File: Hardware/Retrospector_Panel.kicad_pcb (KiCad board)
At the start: 2 copper layers, 60.8 x 128.5 mm, 43 parts, among them J1 Audio_In_L, J10 Feedback_CV, J11 Audio_In_R, J12 Audio_Out_R, J13 Audio_Out_L, J2 Delay_CV_L, J7 Mix_CV, J8 Delay_CV_R, J9 Clock

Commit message: Added some test clock code using timer to capture clock interval in capture and compare input mode
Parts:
- removed the Ref** at (143.5, 64.5)
- removed the Ref** at (145.5, 108.5)
- removed the Ref** at (114.5, 108.5)
- removed the Ref** at (130.0, 86.5)
- added DELAY_L: Alpha_9mm_pot_hole, Custom_Footprints:Alpha_9mm_pot_hole, B.Cu at (143.5, 64.5)
- added FEEDBACK: Alpha_9mm_pot_hole, Custom_Footprints:Alpha_9mm_pot_hole, B.Cu at (145.5, 108.5)
- added MIX: Alpha_9mm_pot_hole, Custom_Footprints:Alpha_9mm_pot_hole, B.Cu at (114.5, 108.5)
- added TONE: Alpha_9mm_pot_hole, Custom_Footprints:Alpha_9mm_pot_hole, B.Cu at (130.0, 86.5)
- LED_L, LED_R: renamed from Ref**; footprint Custom_Footprints:Sub_Miniature_Switch_MountingHole_3mm -> Custom_Footprints:LED_Hole_3mm; moved to B.Cu
- MODE, TYPE: renamed from Ref**; moved to B.Cu
- RESET: renamed from Ref**; footprint Custom_Footprints:Sub_Miniature_Switch_MountingHole_3.5mm -> Custom_Footprints:Small_Pushbutton_Hole_3.5mm; moved to B.Cu
- Ref** (x9): moved to B.Cu
- moved D1 536.5 mm to (-267.1, 49.5)
- moved D2 536.5 mm to (-316.6, 49.5)
- moved Delay_Pot_L1 536.5 mm to (-279.6, 63.5)
- moved Delay_Pot_R1 536.5 mm to (-306.6, 63.5)
- moved FXMODE1 536.5 mm to (-307.6, 75.4)
- moved FXTYPE1 536.5 mm to (-274.6, 80.5)
- moved Feedback_Pot1 536.5 mm to (-277.6, 107.5)
- moved J1 536.5 mm to (-269.6, 142.5)
- moved J10 536.5 mm to (-280.1, 125.5)
- moved J11 536.5 mm to (-280.1, 142.5)
- moved J12 536.5 mm to (-311.6, 142.5)
- moved J13 536.5 mm to (-301.1, 142.5)
- moved J2 536.5 mm to (-269.6, 125.5)
- moved J7 536.5 mm to (-301.1, 125.5)
- moved J8 536.5 mm to (-311.6, 125.5)
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- renumbered Ref** to DELAY_R
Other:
- board text removed: "Delay knobs Large unskirted 15.5mm base diameter"
- board text removed: "Mix/Feedback knobs small skirted 14.2mm base diameter"

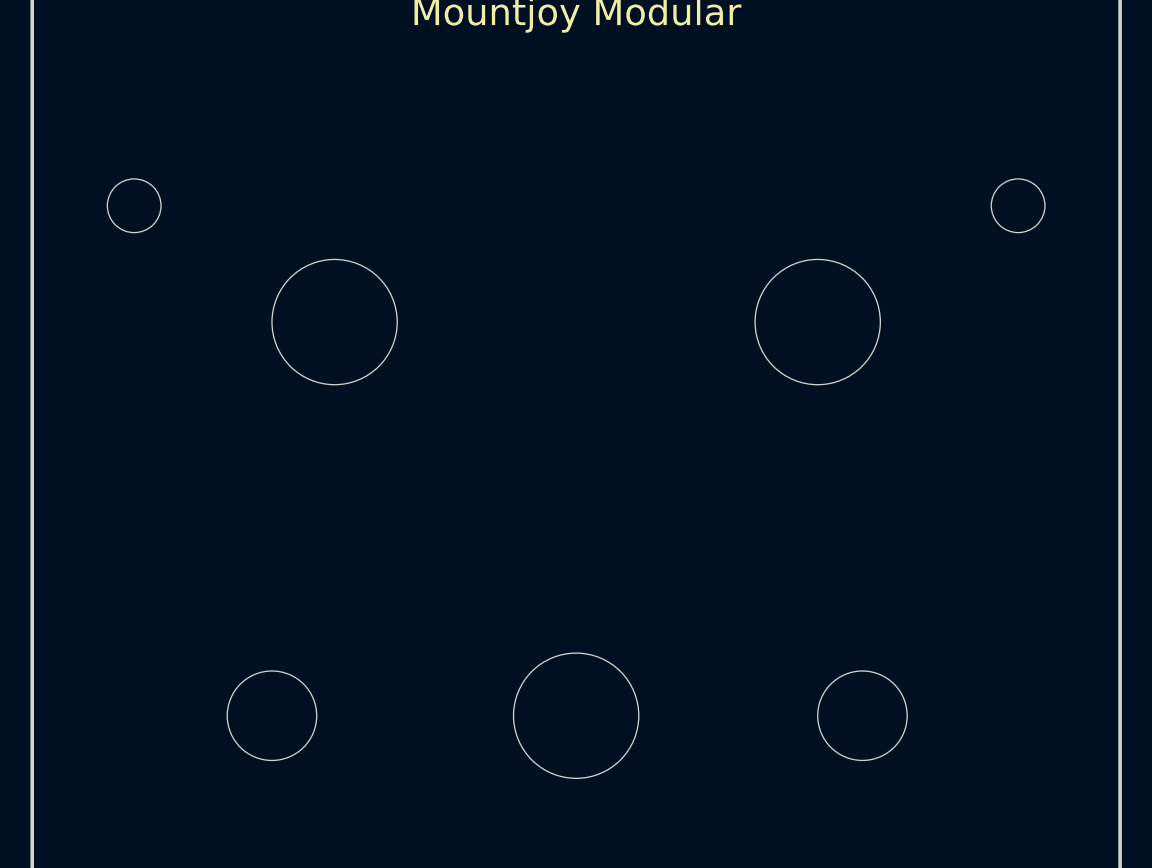
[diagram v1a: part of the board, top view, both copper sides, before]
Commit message: Panel and Control PCB Updates
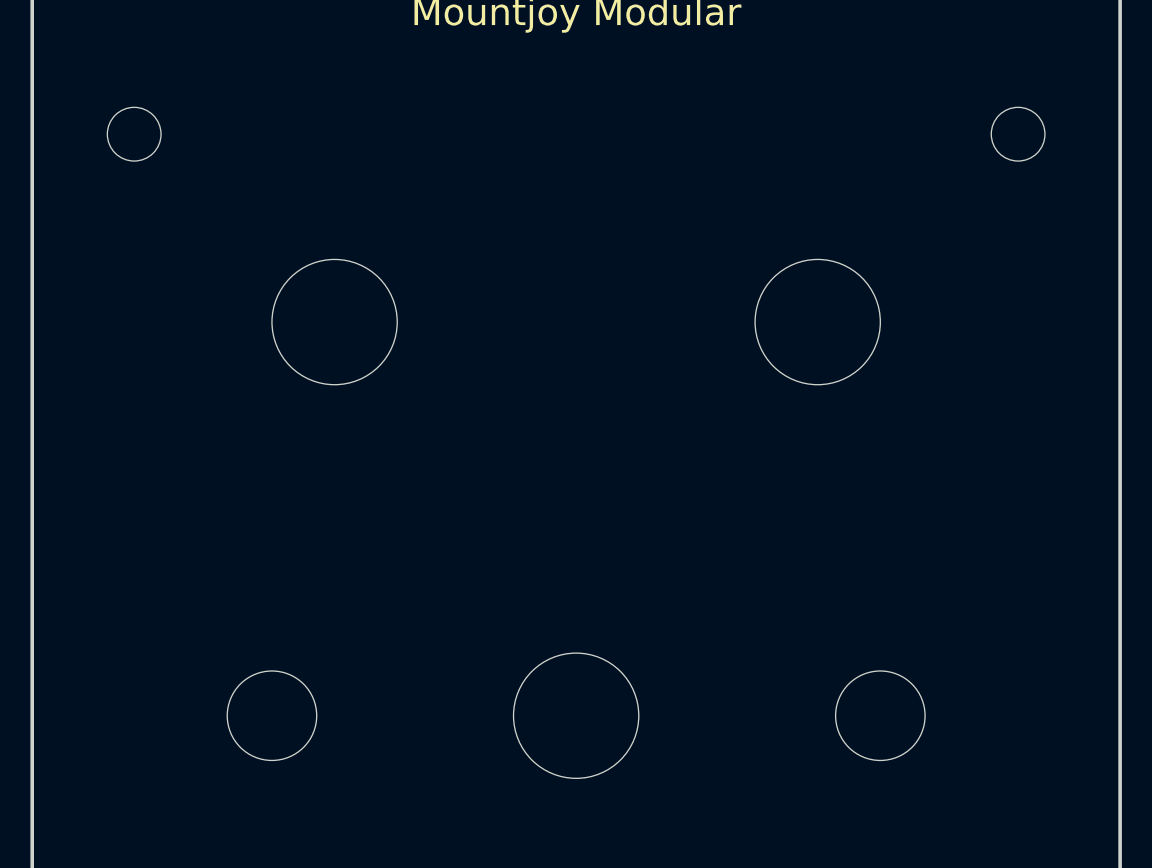
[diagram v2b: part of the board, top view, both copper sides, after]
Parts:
- moved LED_L 4.00 mm to (154.7, 54.0)
- moved LED_R 4.00 mm to (105.3, 54.0)
- moved MODE 1.00 mm to (147.0, 86.5)
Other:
- board text added: "Wet/Dry"
- board text removed: "Delay"
- board text removed: "FB"
- board text removed: "Mix"
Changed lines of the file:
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@@
   (general
     (thickness 1.6)
-    (drawings 68)
+    (drawings 75)
     (tracks 0)
     (zones 0)
@@
   )
   (module Custom_Footprints:Sub_Miniature_Switch_MountingHole_5mm (layer B.Cu)
-    (at 146 86.5)
+    (at 147 86.5)
     (descr "Mounting Hole 6mm, no annular")
     (tags "mounting hole 6mm no annular")
@@
   )
   (module Custom_Footprints:LED_Hole_3mm (layer B.Cu)
-    (at 105.3 58)
+    (at 105.3 54)
     (descr "Mounting Hole 6mm, no annular")
     (tags "mounting hole 6mm no annular")
@@
   )
   (module Custom_Footprints:LED_Hole_3mm (layer B.Cu)
-    (at 154.7 58)
+    (at 154.7 54)
     (descr "Mounting Hole 6mm, no annular")
     (tags "mounting hole 6mm no annular")
@@
     )
   )
-  (gr_line (start 127.5 73) (end 132.5 73) (layer B.Mask) (width 0.4))
-  (gr_line (start 120 76) (end 127.5 73) (layer B.Mask) (width 0.4))
-  (gr_line (start 132.5 73) (end 140 76) (layer B.Mask) (width 0.4))
-  (gr_line (start 120 76) (end 100 76) (layer B.Mask) (width 0.4))
-  (gr_line (start 120 125.5) (end 100 125.5) (layer B.Mask) (width 0.4))
-  (gr_line (start 159.5 125.5) (end 140 125.5) (layer B.Mask) (width 0.4))
-  (gr_line (start 140 125.5) (end 130 123.5) (layer B.Mask) (width 0.4))
-  (gr_line (start 130 123.5) (end 120 125.5) (layer B.Mask) (width 0.4))
-  (gr_line (start 130 51) (end 140 49) (layer B.Mask) (width 0.4))
-  (gr_line (start 120 49) (end 130 51) (layer B.Mask) (width 0.4))
-  (gr_line (start 140 49) (end 160 49) (layer B.Mask) (width 0.4))
-  (gr_line (start 100.5 49) (end 120 49) (layer B.Mask) (width 0.4))
-  (gr_line (start 159.5 76) (end 140 76) (layer B.Mask) (width 0.4))
-  (gr_poly (pts (xy 125 156.9) (xy 103 156.9) (xy 103 145) (xy 125 145)) (layer B.Mask) (width 0.1))
+  (gr_line (start 118.5 77) (end 100 77) (layer B.Mask) (width 0.4))
+  (gr_arc (start 118 63) (end 118 77) (angle -56.08256946) (layer B.Mask) (width 0.4))
+  (gr_arc (start 142.7 63) (end 142.7 49) (angle -180) (layer B.Mask) (width 0.4))
+  (gr_arc (start 118 63.080128) (end 129.6 55.1) (angle -55.47428124) (layer B.Mask) (width 0.4))
+  (gr_line (start 100.5 49) (end 118 49) (layer B.Mask) (width 0.4))
+  (gr_line (start 142 49) (end 160 49) (layer B.Mask) (width 0.4))
+  (gr_line (start 159.5 77) (end 142 77) (layer B.Mask) (width 0.4))
+  (gr_line (start 160.5 96) (end 148.5 96) (layer B.Mask) (width 0.4))
+  (gr_line (start 112 96.08617) (end 100 96.08617) (layer B.Mask) (width 0.4))
+  (gr_line (start 140.5 115) (end 145.5 108.5) (layer B.Mask) (width 0.4))
+  (gr_poly (pts (xy 124 157) (xy 104 157) (xy 104 156) (xy 124 156)) (layer B.Mask) (width 0.1))
+  (gr_poly (pts (xy 124 146.5) (xy 104 146.5) (xy 104 145.5) (xy 124 145.5)) (layer B.Mask) (width 0.1))
+  (gr_circle (center 124 156) (end 124.5 156) (layer B.Mask) (width 1))
+  (gr_circle (center 124 146.5) (end 124.5 146.5) (layer B.Mask) (width 1))
+  (gr_circle (center 104 156) (end 104.5 156) (layer B.Mask) (width 1))
+  (gr_circle (center 104 146.5) (end 104.5 146.5) (layer B.Mask) (width 1))
+  (gr_arc (start 112.000001 111.999999) (end 123 100.5) (angle -43.72697345) (layer B.Mask) (width 0.4))
+  (gr_arc (start 148.100593 111.904836) (end 148.5 96) (angle -45.21155789) (layer B.Mask) (width 0.4))
+  (gr_arc (start 130 93) (end 123 100.5) (angle -86.75204533) (layer B.Mask) (width 0.4))
+  (gr_line (start 114.5 108.5) (end 119.5 115) (layer B.Mask) (width 0.4))
+  (gr_line (start 119.5 115) (end 119.5 134.3) (layer B.Mask) (width 0.4))
+  (gr_line (start 140.5 134) (end 140.5 115) (layer B.Mask) (width 0.4))
+  (gr_line (start 140 150.9) (end 151 150.9) (layer B.Mask) (width 0.4))
+  (gr_line (start 100 162.5) (end 160.25 162.5) (layer B.Mask) (width 0.4))
+  (gr_poly (pts (xy 125 156) (xy 103 156) (xy 103 146.5) (xy 125 146.5)) (layer B.Mask) (width 0.1))
   (gr_line (start -260.2 160.8) (end -260.2 158.7) (layer Cmts.User) (width 0.15))
   (gr_line (start -262.3 160.8) (end -260.2 160.8) (layer Cmts.User) (width 0.15))
@@
     (effects (font (size 1 1) (thickness 0.15)) (justify mirror))
   )
-  (gr_text Reset (at 130 115) (layer B.Mask)
+  (gr_text Reset (at 130 113.5) (layer B.Mask)
     (effects (font (size 1.5 1.5) (thickness 0.15)) (justify mirror))
   )
@@
     (effects (font (size 2 2) (thickness 0.3)) (justify mirror))
   )
-  (gr_text Mix (at 119.5 142) (layer B.Mask)
-    (effects (font (size 2 2) (thickness 0.3)) (justify mirror))
-  )
-  (gr_text FB (at 140.5 142) (layer B.Mask)
-    (effects (font (size 2 2) (thickness 0.3)) (justify mirror))
-  )
   (gr_text "Del R" (at 108 142) (layer B.Mask)
     (effects (font (size 2 2) (thickness 0.3)) (justify mirror))
@@
     (effects (font (size 2 2) (thickness 0.3)) (justify mirror))
   )
-  (gr_text Mix (at 114.8 119.9) (layer B.Mask)
+  (gr_text Wet/Dry (at 111 118.5) (layer B.Mask)
     (effects (font (size 2 2) (thickness 0.3)) (justify mirror))
   )
-  (gr_text Feedback (at 145.8 119.9) (layer B.Mask)
+  (gr_text Feedback (at 150 118) (layer B.Mask)
     (effects (font (size 2 2) (thickness 0.3)) (justify mirror))
   )
-  (gr_text Mode (at 113.2 93) (layer B.Mask)
+  (gr_text Mode (at 104.5 86.5 90) (layer B.Mask)
     (effects (font (size 2 2) (thickness 0.3)) (justify mirror))
   )
-  (gr_text DFX (at 146.2 93.2) (layer B.Mask)
-    (effects (font (size 2 2) (thickness 0.3)) (justify mirror))
-  )
-  (gr_text Delay (at 146.2 80) (layer B.Mask)
+  (gr_text DFX (at 155.5 86 270) (layer B.Mask)
     (effects (font (size 2 2) (thickness 0.3)) (justify mirror))
   )
@@
     (effects (font (size 2 2) (thickness 0.3)) (justify mirror))
   )
-  (gr_text "Delay R" (at 116.5 53.5) (layer B.Mask)
+  (gr_text "Delay R" (at 116 54) (layer B.Mask)
     (effects (font (size 2 2) (thickness 0.3)) (justify mirror))
   )
-  (gr_text "Delay L" (at 143 53.5) (layer B.Mask)
+  (gr_text "Delay L" (at 143.5 54) (layer B.Mask)
     (effects (font (size 2 2) (thickness 0.3)) (justify mirror))
   )
@@
     (effects (font (size 1.5 1.5) (thickness 0.3)))
   )
-  (gr_line (start 130 50) (end 130 160) (layer Dwgs.User) (width 0.05))
   (gr_line (start 160 50) (end 160 160) (layer Dwgs.User) (width 0.2))
   (gr_line (start 100 160) (end 160 160) (layer Dwgs.User) (width 0.2))

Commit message: Final changes to PCBs for manufacture
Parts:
- removed D1, D2: LED, LEDs:LED_D3.0mm
- removed Delay_Pot_L1, Delay_Pot_R1, Feedback_Pot1, Mix_Pot1, Tone_Pot1: A10k, Custom_Footprints:Alpha_9mm_Potentiometer
- removed FXMODE1: SW_SPDT_MSM, Custom_Footprints:SPDTSubMiniature
- removed FXTYPE1: SW_SPST, Custom_Footprints:SPDTSubMiniature
- removed J1: Audio_In_L, Custom_Footprints:THONKICONN_hole
- removed J10: Feedback_CV, Custom_Footprints:THONKICONN_hole
- removed J11: Audio_In_R, Custom_Footprints:THONKICONN_hole
- removed J12: Audio_Out_R, Custom_Footprints:THONKICONN_hole
- removed J13: Audio_Out_L, Custom_Footprints:THONKICONN_hole
- removed J2: Delay_CV_L, Custom_Footprints:THONKICONN_hole
- removed J7: Mix_CV, Custom_Footprints:THONKICONN_hole
- removed J8: Delay_CV_R, Custom_Footprints:THONKICONN_hole
- removed J9: Clock, Custom_Footprints:THONKICONN_hole
- removed RESET1: SW_Push, Buttons_Switches_THT:SW_PUSH_6mm
- moved DELAY_L 0.50 mm to (144.0, 64.5)
- moved DELAY_R 0.50 mm to (116.0, 64.5)
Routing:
- added copper zone on F.Cu, net (none)
- removed copper zone on B.Cu, net GND

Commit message: Updates to Panel layout
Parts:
- removed the Ref** at (130.0, 134.0)
- added LED_R: Subminiature_Switch, Custom_Footprints:LED_Hole_3mm, B.Cu at (130.0, 97.8)
- added RESET: Subminiature_Switch, Custom_Footprints:Small_Pushbutton_Hole_3.5mm, B.Cu at (130.0, 64.5)
- added Ref**: Thonkiconn_Socket_MountingHole_6mm, Custom_Footprints:Thonkiconn_Socket_MountingHole_6mm, B.Cu at (130.0, 127.0)
- added Ref**: Thonkiconn_Socket_MountingHole_6mm, Custom_Footprints:Thonkiconn_Socket_MountingHole_6mm, B.Cu at (130.0, 151.0)
- added TYPE: Subminiature_Switch, Custom_Footprints:Sub_Miniature_Switch_MountingHole_5mm, B.Cu at (130.0, 110.3)
- moved RESET 29.9 mm to (130.0, 138.4)
- moved MODE 2.70 mm to (149.7, 86.5)
- moved TYPE 2.40 mm to (110.6, 86.5)
- moved DELAY_L 1.50 mm to (145.5, 64.5)
- moved DELAY_R 1.50 mm to (114.5, 64.5)
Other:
- board text added: "Chorus"
- board text added: "Dry/Wet"
- board text added: "Filter"
- board text added: "Link"
- board text added: "Retrospector Panel v2 Mountjoy Modular"
- board text added: "Reverse"
- board text added: "Short"
- board text added: "Wide"
- board text removed: "DFX"
- board text removed: "Mode"
- board text removed: "Retrospector Panel v1 Mountjoy Modular"
- board text removed: "Tone"
- board text removed: "Wet/Dry"

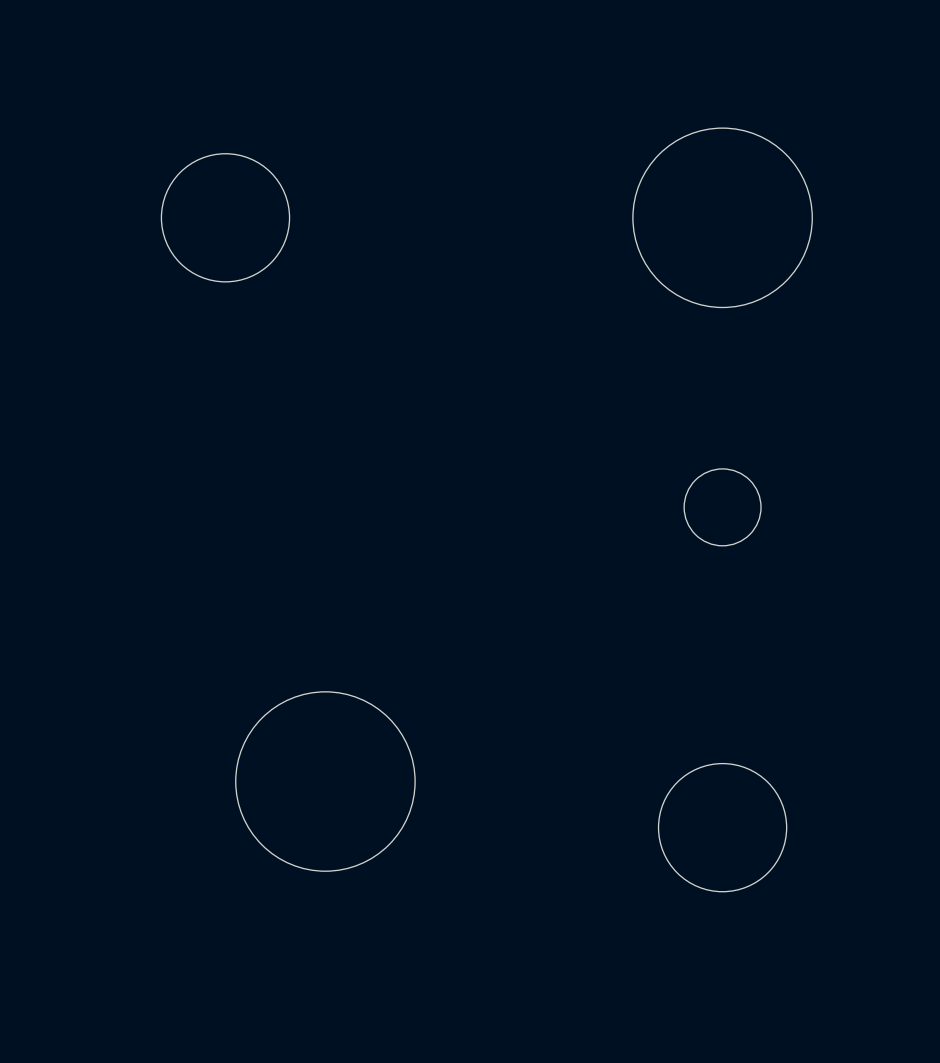
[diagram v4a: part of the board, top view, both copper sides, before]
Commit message: Routed controls PCB
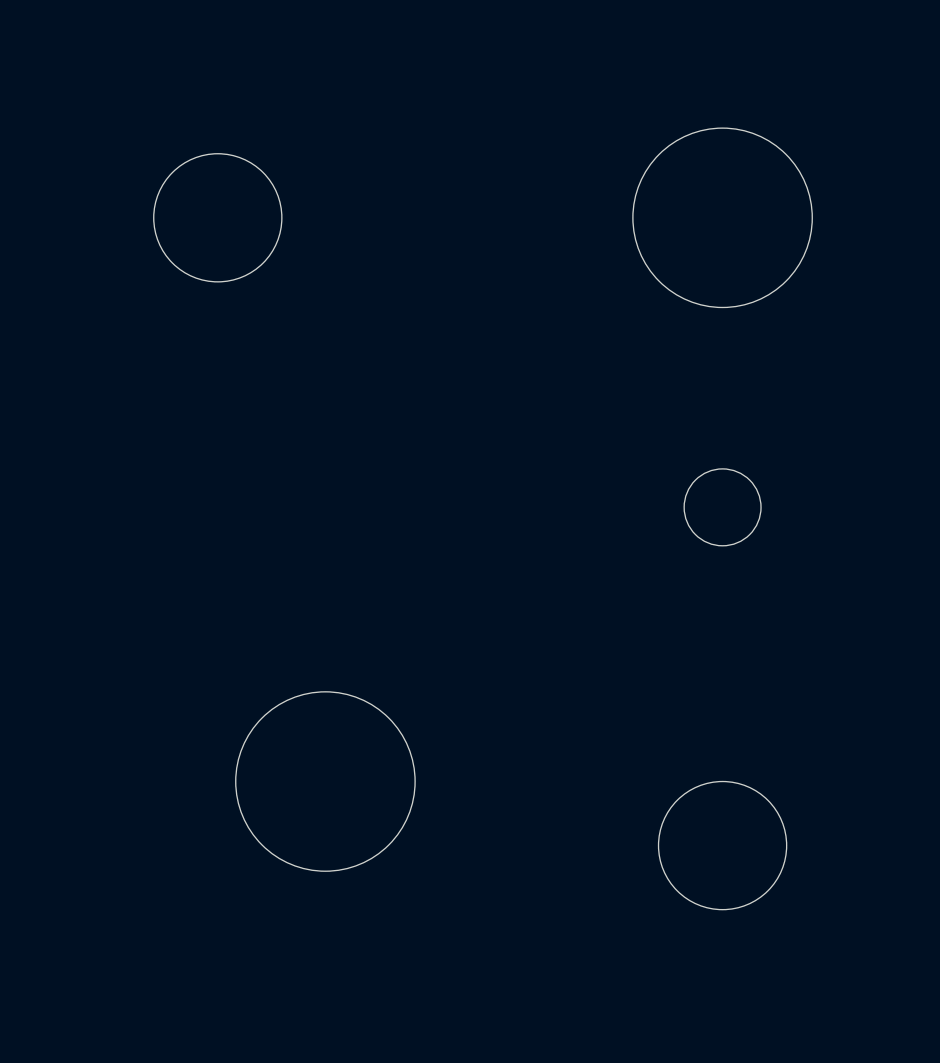
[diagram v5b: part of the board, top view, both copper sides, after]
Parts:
- moved TYPE 0.70 mm to (130.0, 111.0), turned to 90 degrees
- moved TYPE 0.30 mm to (110.3, 86.5)
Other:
- board text added: "HP"
- board text added: "LP"
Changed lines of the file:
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@@
   (general
     (thickness 1.6)
-    (drawings 71)
+    (drawings 73)
     (tracks 0)
     (zones 0)
@@
     (solder_mask_min_width 0.25)
     (aux_axis_origin 0 0)
-    (visible_elements 7FEDF77F)
+    (visible_elements 7FFDF77F)
     (pcbplotparams
       (layerselection 0x010f0_ffffffff)
@@
   )
   (module Custom_Footprints:Sub_Miniature_Switch_MountingHole_5mm (layer B.Cu)
-    (at 130 110.3)
-    (descr "Mounting Hole 6mm, no annular")
-    (tags "mounting hole 6mm no annular")
-    (fp_text reference TYPE (at 0 5.4) (layer B.SilkS) hide
-      (effects (font (size 1 1) (thickness 0.15)) (justify mirror))
-    )
-    (fp_text value Subminiature_Switch (at 0 -5.1) (layer B.Fab) hide
+    (at 130 111 90)
+    (descr "Mounting Hole 6mm, no annular")
+    (tags "mounting hole 6mm no annular")
+    (fp_text reference TYPE (at 0 5.4 90) (layer B.SilkS) hide
+      (effects (font (size 1 1) (thickness 0.15)) (justify mirror))
+    )
+    (fp_text value Subminiature_Switch (at 0 -5.1 90) (layer B.Fab) hide
       (effects (font (size 1 1) (thickness 0.15)) (justify mirror))
     )
     (fp_circle (center 0 0) (end 2.5 0) (layer Cmts.User) (width 0.15))
     (fp_circle (center 0 0) (end 4 0) (layer B.CrtYd) (width 0.05))
-    (pad "" np_thru_hole circle (at 0 0) (size 5 5) (drill 5) (layers *.Cu *.Mask))
+    (pad "" np_thru_hole circle (at 0 0 90) (size 5 5) (drill 5) (layers *.Cu *.Mask))
     (model ":custom_3d:Eledis 1A11-NF1STSE SPDT Toggle Switch.stp"
       (offset (xyz 0 3.8 -12))
@@
   )
   (module Custom_Footprints:Sub_Miniature_Switch_MountingHole_5mm (layer B.Cu)
-    (at 110.6 86.5)
+    (at 110.3 86.5)
     (descr "Mounting Hole 6mm, no annular")
     (tags "mounting hole 6mm no annular")
@@
     (pad "" np_thru_hole oval (at 0 0) (size 5 3.2) (drill oval 5 3.2) (layers *.Cu *.Mask))
   )
+  (gr_text HP (at 126.3 104.9) (layer B.Mask)
+    (effects (font (size 2 2) (thickness 0.3)) (justify mirror))
+  )
+  (gr_text LP (at 133.8 104.9) (layer B.Mask)
+    (effects (font (size 2 2) (thickness 0.3)) (justify mirror))
+  )
   (gr_line (start 130 94.8) (end 130 92.5) (layer B.Mask) (width 0.4))
   (gr_line (start 120.5 73.75) (end 99.75 73.75) (layer B.Mask) (width 0.4))
@@
     (effects (font (size 2 2) (thickness 0.3)) (justify mirror))
   )
-  (gr_text Reverse (at 110.7 92.6) (layer B.Mask)
+  (gr_text Reverse (at 110.4 92.6) (layer B.Mask)
     (effects (font (size 2 2) (thickness 0.3)) (justify mirror))
   )
@@
     (effects (font (size 2 2) (thickness 0.3)) (justify mirror))
   )
-  (gr_text Short (at 110.6 80) (layer B.Mask)
-    (effects (font (size 2 2) (thickness 0.3)) (justify mirror))
-  )
+  (gr_text Short (at 110.3 80) (layer B.Mask)
+    (effects (font (size 2 2) (thickness 0.3)) (justify mirror))
+  )
